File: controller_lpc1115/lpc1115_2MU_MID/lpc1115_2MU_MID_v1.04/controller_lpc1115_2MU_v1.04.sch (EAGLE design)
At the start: 59 parts, among them IC1 LPC1115, IC2 BD9G101, Q1 BC856, Q2 BC847C, Q3 BCP52, Q4 ASFL

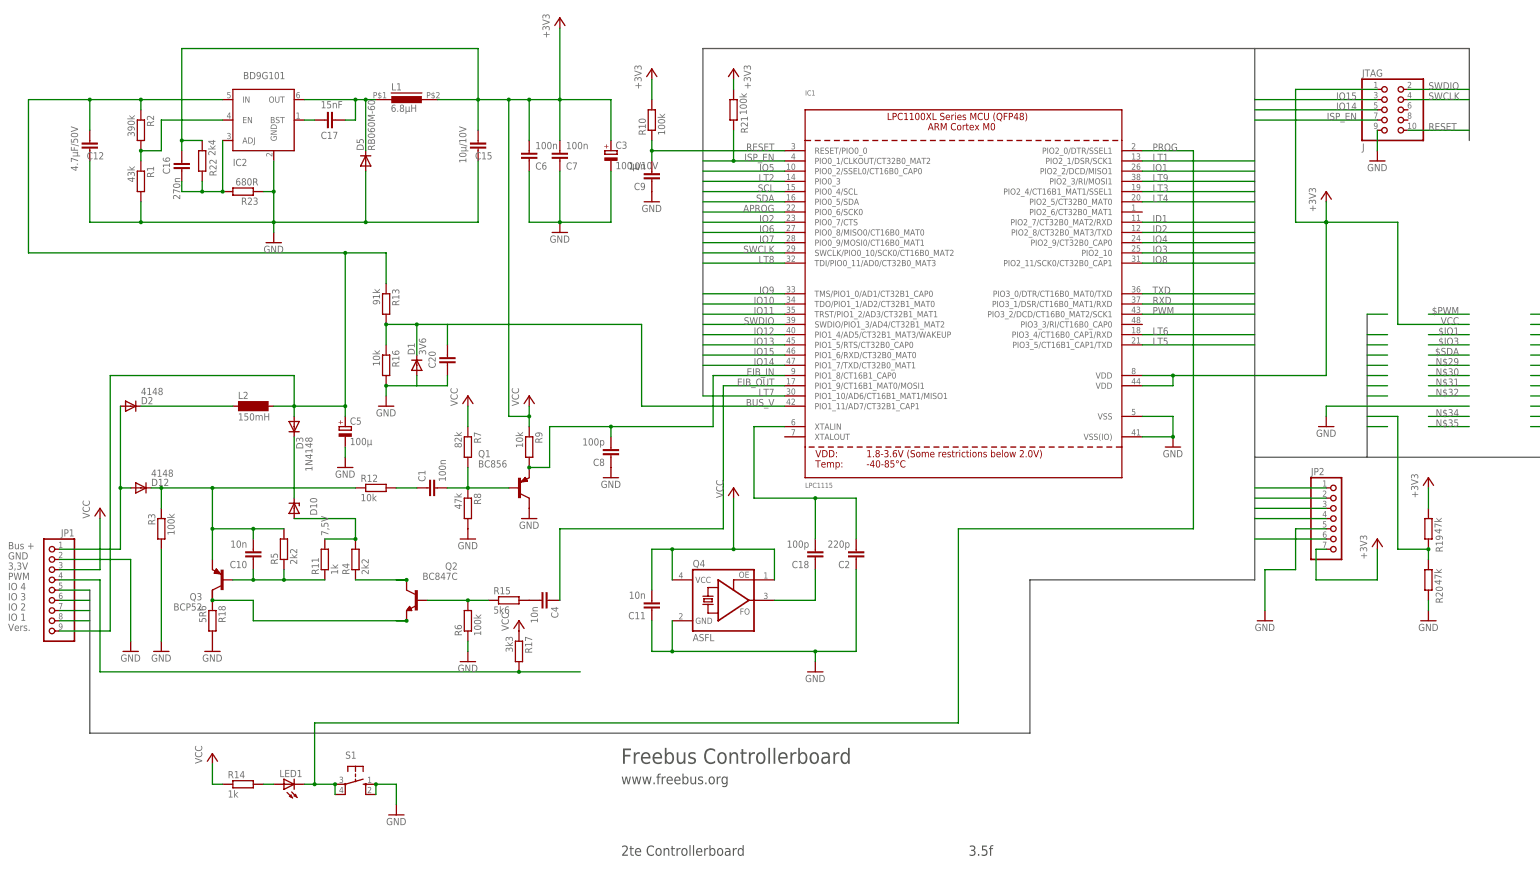
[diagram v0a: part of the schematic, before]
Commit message: Add JP1 and JP2 pininfo for 2MU lpc1115 controller v1.04
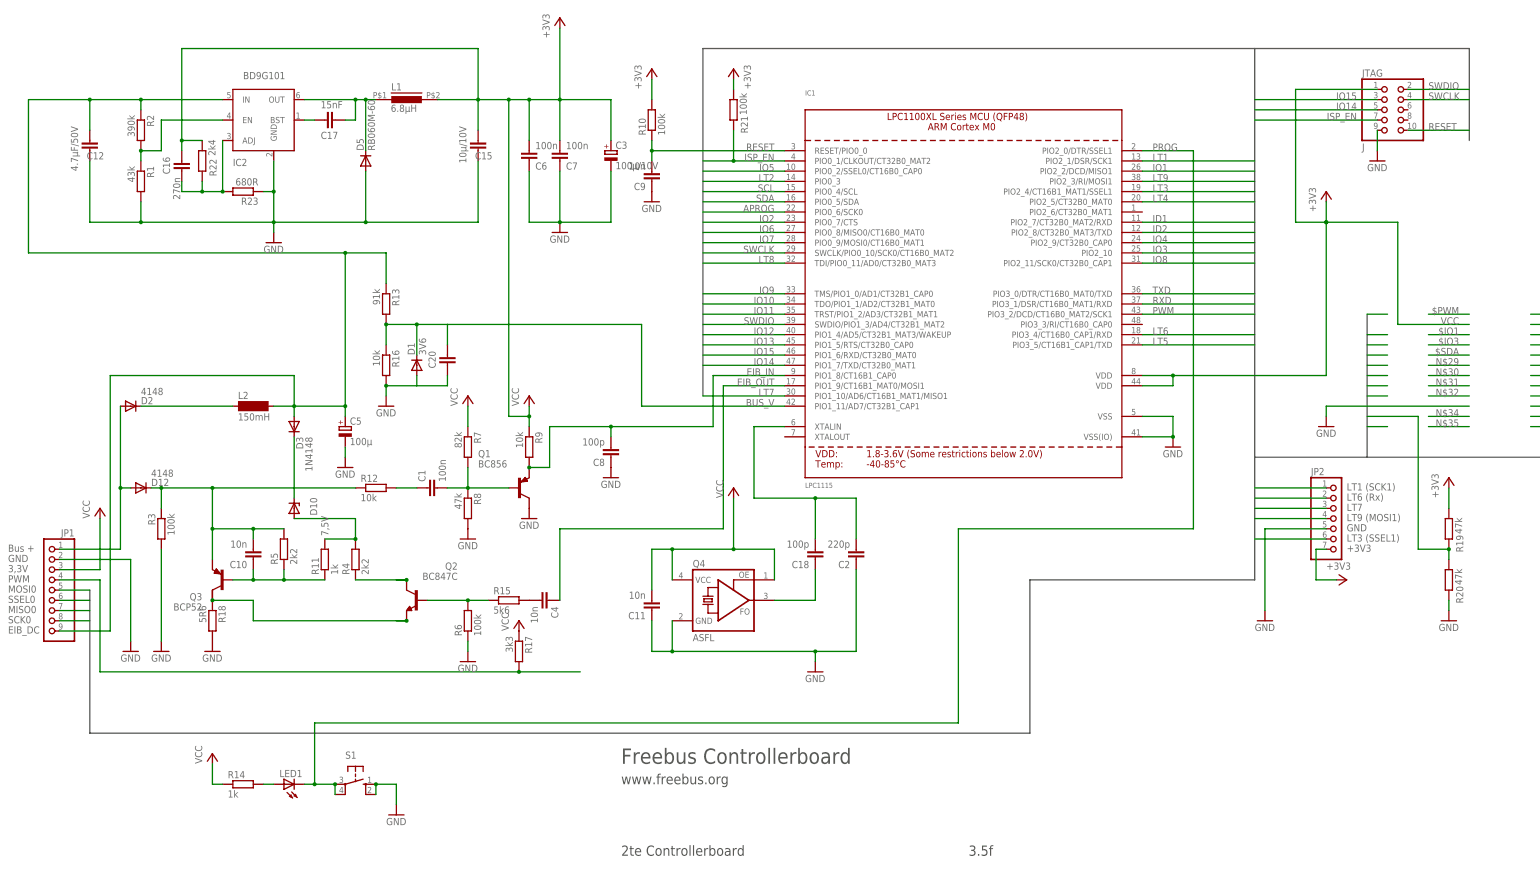
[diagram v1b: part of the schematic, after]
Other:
- note added: "+3V3"
- note added: "EIB_DC"
- note added: "LT1 (SCK1)"
- note added: "LT3 (SSEL1)"
- note added: "LT6 (Rx)"
- note added: "LT7"
- note added: "LT9 (MOSI1)"
- note added: "MISO0"
- note added: "MOSI0"
- note added: "SCK0"
- note added: "SSEL0"
- note removed: "IO 1"
- note removed: "IO 2"
- note removed: "IO 3"
- note removed: "IO 4"
- note removed: "Vers."
- moved on the sheet: R19, R20
